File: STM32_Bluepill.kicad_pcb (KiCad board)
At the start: 2 copper layers, 28 parts, among them J1 USB_B_Micro, J2 Conn_01x04_Male, J3 Conn_01x04_Male, J4 Conn_01x04_Male, U1 STM32F103C8T6, U2 AMS1117-3.3, Y1 16MHz

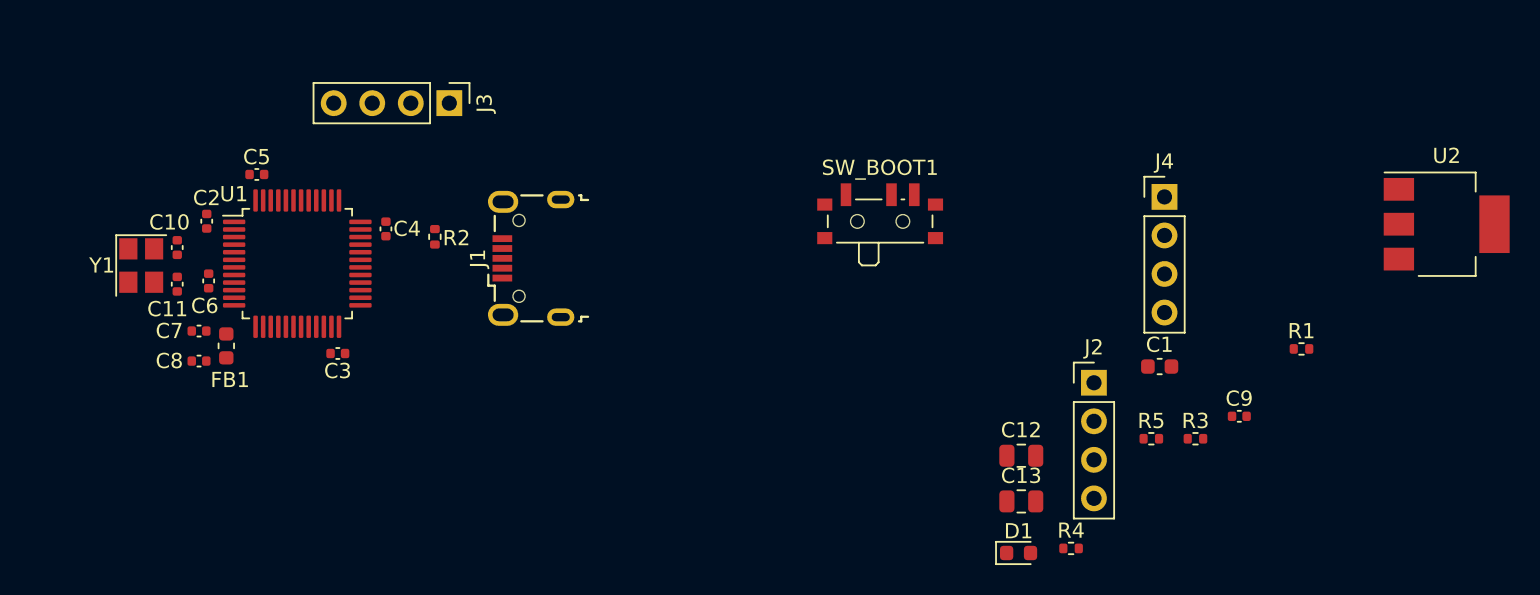
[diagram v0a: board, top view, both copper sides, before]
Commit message: Layout: Place switch and connectors
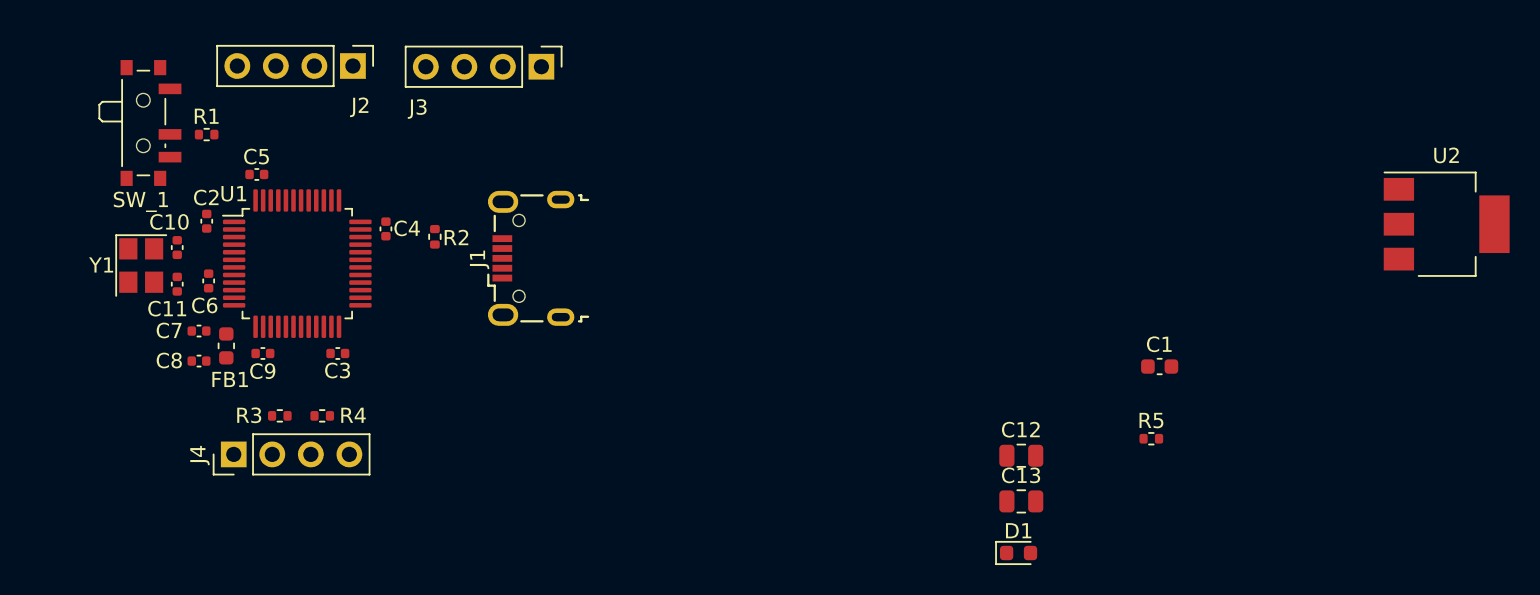
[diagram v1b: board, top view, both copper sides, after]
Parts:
- moved R1 73.5 mm to (170.9, 83.8)
- moved C9 64.5 mm to (174.7, 98.2)
- moved J4 63.7 mm to (172.7, 104.9), turned to 90 degrees
- moved R3 60.4 mm to (175.8, 102.4), turned to 180 degrees
- moved J2 53.1 mm to (180.6, 79.3), turned to -90 degrees
- moved R4 50.1 mm to (178.6, 102.4)
- moved SW_1 48.6 mm to (167.1, 83.1), turned to -90 degrees
- moved J3 6.53 mm to (193.0, 79.3)
- renumbered SW_BOOT1 to SW_1
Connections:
- net Net-(R1-Pad1) renamed /SW_BOOT1

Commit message: Layout: Place power supplies and bulk cap
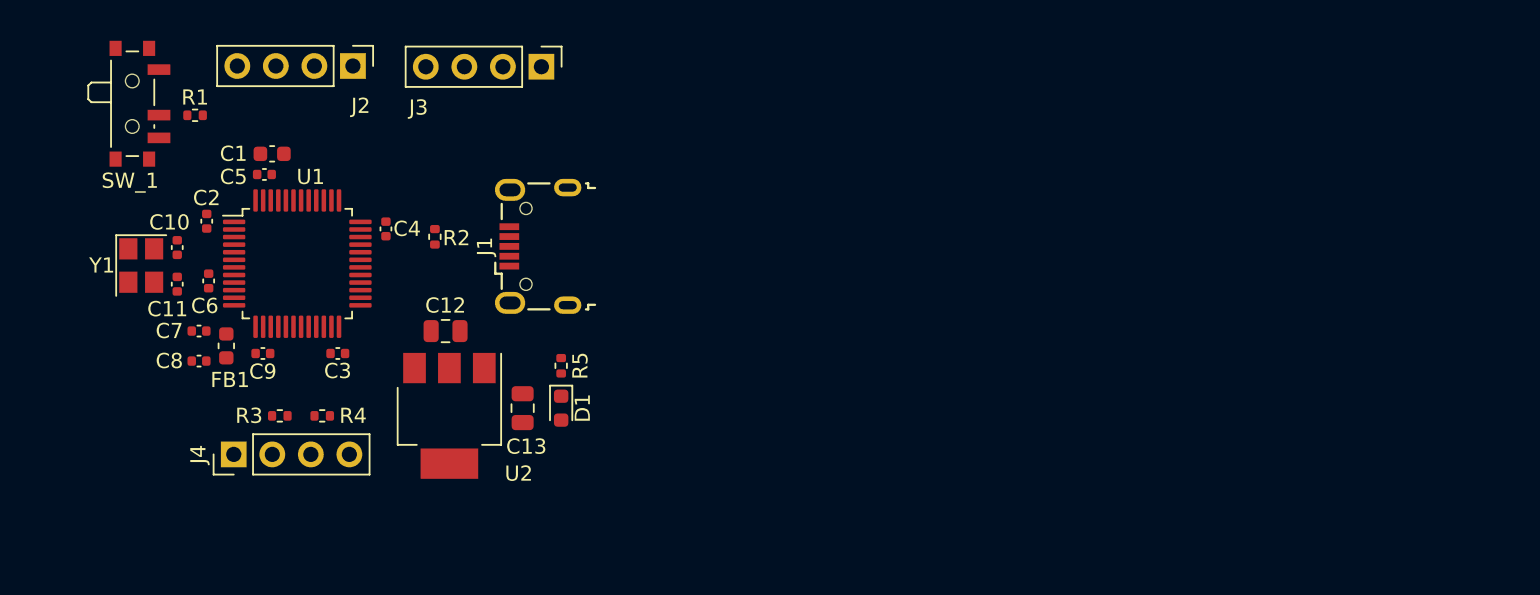
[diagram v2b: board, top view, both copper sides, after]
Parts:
- moved U2 66.9 mm to (186.9, 102.4), turned to -90 degrees
- moved C1 60.2 mm to (175.3, 85.1)
- moved R5 39.2 mm to (194.3, 99.1), turned to 90 degrees
- moved C12 38.8 mm to (186.7, 96.8)
- moved C13 33.4 mm to (191.8, 101.9), turned to 90 degrees
- moved D1 31.6 mm to (194.3, 101.9), turned to -90 degrees
- moved R1 1.48 mm to (170.2, 82.5)
- moved SW_1 1.46 mm to (166.4, 81.8)
- moved J1 0.91 mm to (192.8, 91.2)
- moved C5 0.50 mm to (174.8, 86.5)

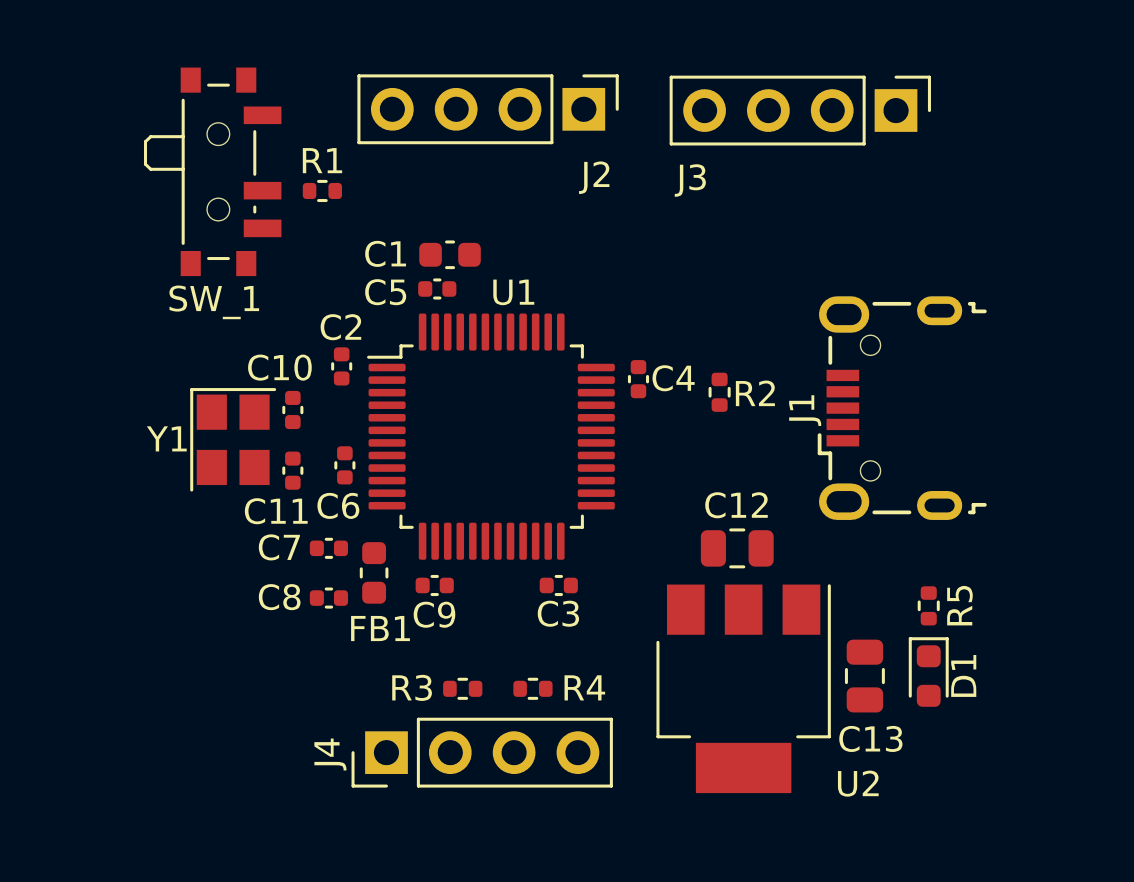
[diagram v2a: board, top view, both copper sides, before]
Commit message: Layout: Add mounting holes and edge cuts
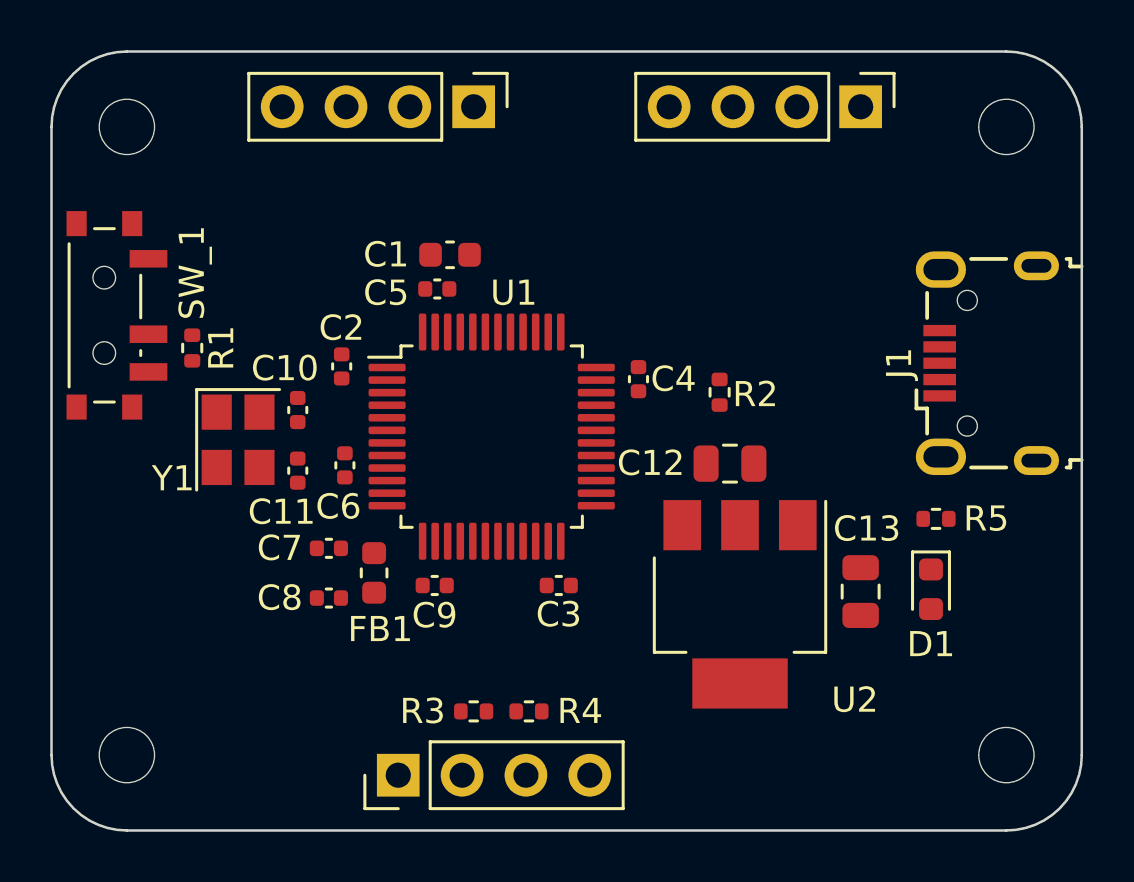
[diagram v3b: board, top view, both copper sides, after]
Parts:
- added H1: MountingHole, MountingHole:MountingHole_2.2mm_M2, F.Cu at (162.4, 105.0)
- added H2: MountingHole, MountingHole:MountingHole_2.2mm_M2, F.Cu at (197.4, 105.0)
- added H3: MountingHole, MountingHole:MountingHole_2.2mm_M2, F.Cu at (197.4, 80.0)
- added H4: MountingHole, MountingHole:MountingHole_2.2mm_M2, F.Cu at (162.4, 80.0)
- moved R1 8.12 mm to (165.0, 88.8), turned to -90 degrees
- moved SW_1 7.30 mm to (161.8, 87.5)
- moved J2 4.39 mm to (176.2, 79.2)
- moved J1 4.25 mm to (196.6, 89.4)
- moved R5 3.47 mm to (194.6, 95.6), turned to 180 degrees
- moved D1 3.46 mm to (194.4, 98.4)
- moved C12 3.39 mm to (186.4, 93.4)
- moved C13 3.37 mm to (191.6, 98.5)
- moved U2 3.37 mm to (186.8, 99.0)
- moved J3 1.42 mm to (191.6, 79.2)
- moved J4 1.01 mm to (173.2, 105.8)
- moved R3 1.00 mm to (176.2, 103.3)
- moved R4 0.91 mm to (178.4, 103.3)
- moved C10 0.20 mm to (169.2, 91.3)
- moved C11 0.20 mm to (169.2, 93.7)
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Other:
- board outline added: 41 x 31 mm

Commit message: Routing: Do ground pour
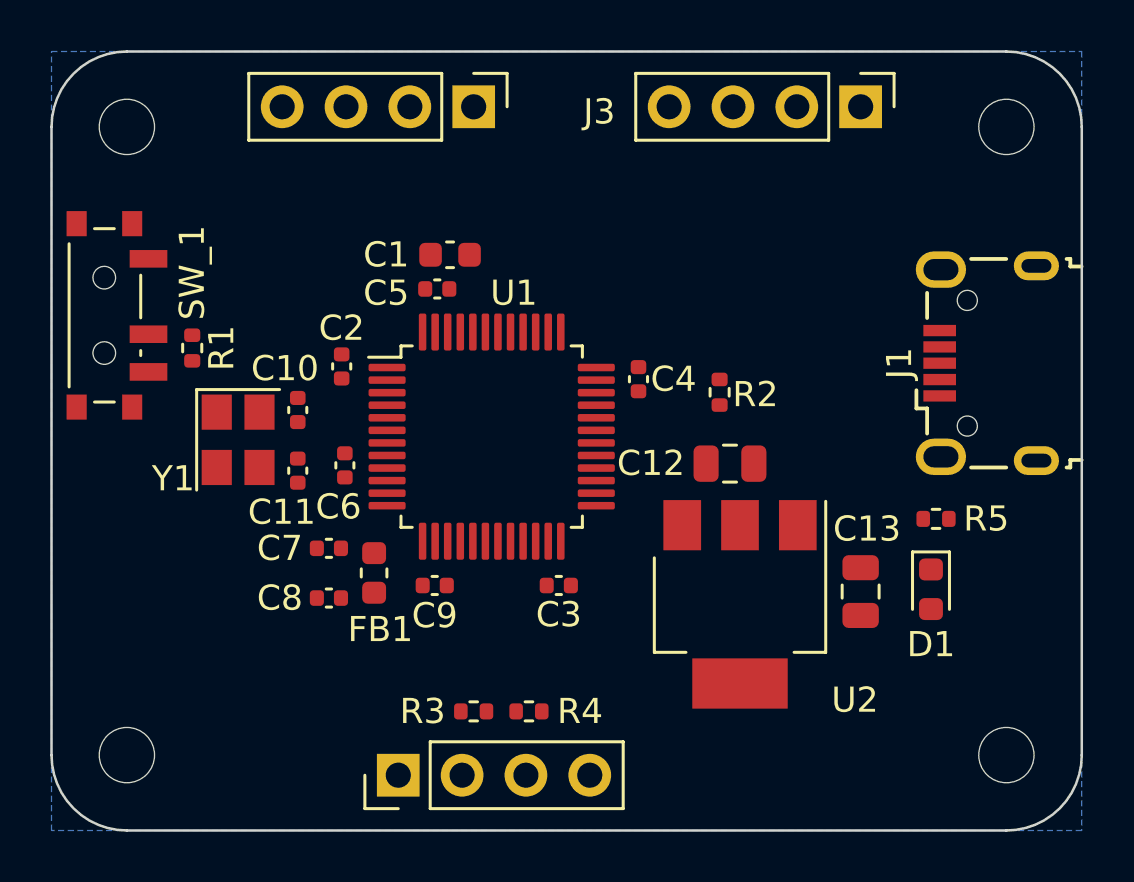
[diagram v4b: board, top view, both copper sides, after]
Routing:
- added copper zone on B.Cu, net GND
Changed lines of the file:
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@@
     (property "Sheetname" "")
     (attr through_hole)
-    (fp_text reference "J3" (at 0.2 10.4) (layer "F.SilkS") hide
+    (fp_text reference "J3" (at 0.2 10.4) (layer "F.SilkS")
       (effects (font (size 1 1) (thickness 0.15)))
     )
@@
   (gr_arc (start 159.4 80) (mid 160.27868 77.87868) (end 162.4 77) (layer "Edge.Cuts") (width 0.1))
   (gr_line (start 159.4 105) (end 159.4 80) (layer "Edge.Cuts") (width 0.1))
+  (zone (net 2) (net_name "GND") (layer "B.Cu") (hatch edge 0.508)
+    (connect_pads (clearance 0.3))
+    (min_thickness 0.25) (filled_areas_thickness no)
+    (fill yes (thermal_gap 0.5) (thermal_bridge_width 0.5))
+    (polygon
+      (pts
+        (xy 200.4 108)
+        (xy 159.4 108)
+        (xy 159.4 77)
+        (xy 200.4 77)
+      )
+    )
+  )
 )

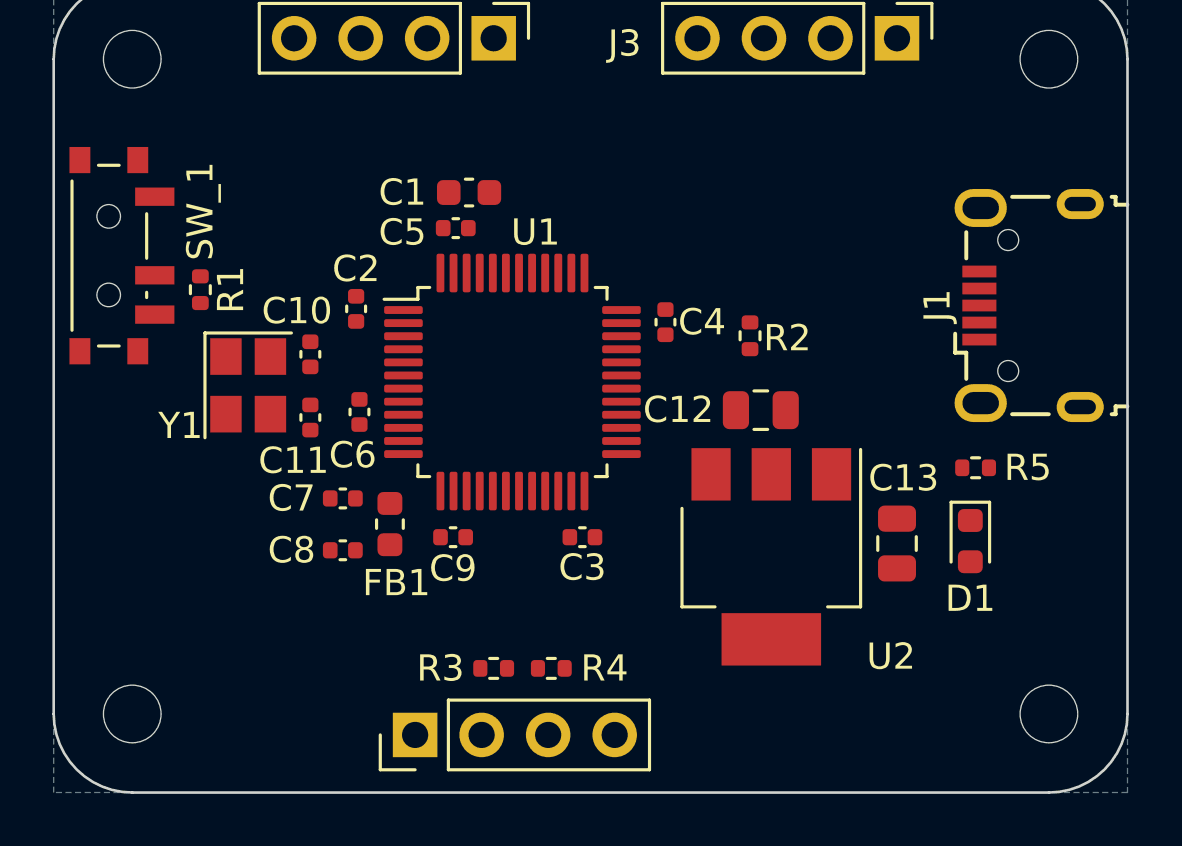
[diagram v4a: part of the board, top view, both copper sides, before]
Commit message: Routing: Route decoupling caps first then XTL HSE_IN/OUT
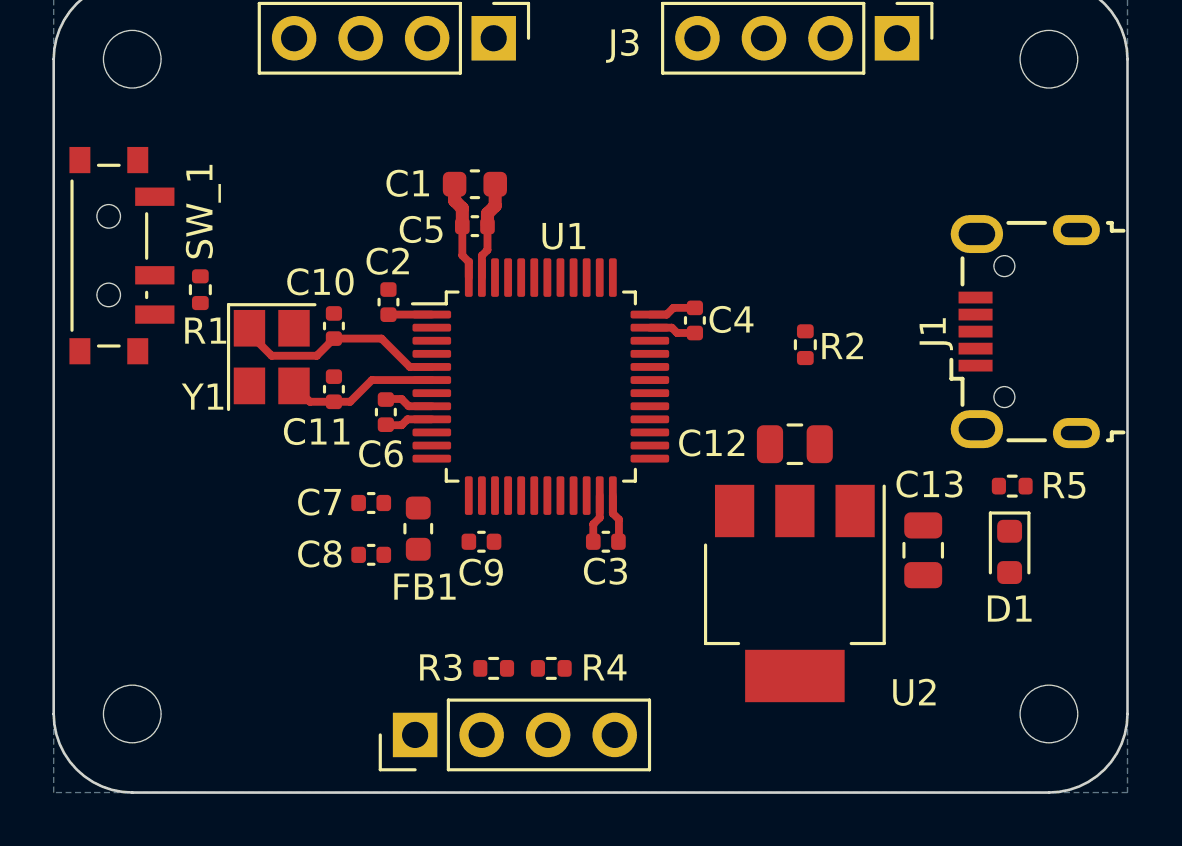
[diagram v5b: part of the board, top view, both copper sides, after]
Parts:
- moved R2 2.14 mm to (188.1, 90.9)
- moved C12 1.84 mm to (187.7, 94.7)
- moved U2 1.66 mm to (187.7, 100.4)
- moved R5 1.57 mm to (196.0, 96.3)
- moved D1 1.56 mm to (195.9, 98.8)
- moved C11 1.41 mm to (170.1, 92.6)
- moved C10 1.41 mm to (170.1, 90.2)
- moved Y1 1.41 mm to (167.7, 91.4)
- moved C2 1.26 mm to (172.2, 89.3)
- moved C4 1.13 mm to (183.9, 90.0)
- moved C8 1.10 mm to (171.5, 98.9)
- moved C9 1.10 mm to (175.7, 98.4)
- moved FB1 1.10 mm to (173.3, 97.9)
- moved U1 1.10 mm to (178.0, 92.5)
- moved C7 1.10 mm to (171.5, 96.9)
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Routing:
- net GND: track 0.00 -> 9.35 mm
- net +3.3V: track 0.00 -> 9.14 mm
- net /HSE_IN: track 0.00 -> 8.24 mm
- net /HSE_OUT: track 0.00 -> 5.86 mm
- net +3.3VA: track 0.00 -> 1.88 mm

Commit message: Routing: Route signals
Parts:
- moved C3 1.78 mm to (182.0, 97.5)
- moved C2 1.58 mm to (173.5, 88.4)
- moved C6 1.58 mm to (173.4, 92.6)
- moved C8 1.58 mm to (172.8, 98.0)
- moved FB1 1.58 mm to (174.6, 97.0)
- moved U1 1.58 mm to (179.3, 91.6)
- moved Y1 1.58 mm to (169.0, 90.5)
- moved C10 1.58 mm to (171.4, 89.3)
- moved C11 1.58 mm to (171.4, 91.7)
- moved C7 1.58 mm to (172.8, 96.0)
- moved C1 1.58 mm to (176.8, 83.9)
- moved C4 1.58 mm to (185.2, 89.1)
- moved C9 1.58 mm to (177.0, 97.5)
- moved C5 1.58 mm to (176.8, 85.5)
- moved R2 1.33 mm to (188.3, 89.6)
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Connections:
- net /SW_BOOT1 renamed /SW_BOOT0
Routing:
- net /BOOT0: track 0.00 -> 20.6 mm
- net /USART1_RX: track 0.00 -> 17.0 mm
- net /USART1_TX: track 0.00 -> 15.4 mm
- net /SWDIO: track 0.00 -> 14.5 mm
- net /I2C2_SCL: track 0.00 -> 12.2 mm
- net /I2C2_SDA: track 0.00 -> 11.2 mm
- net /USB_D-: track 0.00 -> 11.2 mm
- net /USB_D+: track 0.00 -> 11.2 mm
- net /SWCLK: track 0.00 -> 10.1 mm
- net /SW_BOOT0: track 0.00 -> 1.80 mm
